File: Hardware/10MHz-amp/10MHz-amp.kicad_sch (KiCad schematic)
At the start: 122 parts, among them J1 Conn_Coaxial, J2 BANANA_JACK, J3 BANANA_JACK, J4 BANANA_JACK, J5 Conn_Coaxial, J6 Barrel_Jack_MountingPin, J7 Conn_01x07_Pin, J8 Conn_01x07_Socket, K1 TQ2-24V, K2 TQ2-24V, K3 TQ2-24V, K4 TQ2-24V, K5 TQ2-24V, K6 TQ2-5V, Q1 DMPH6250SQ-13, Q2 DMN6075SQ-7, Q4 DMPH6250SQ-13, SW1 SW_SPDT, SW2 SW_SPST, SW3 SW_SP5T_NR01105, SW5 100SP2T1B1M1QEH, U1 THS3491xDDA

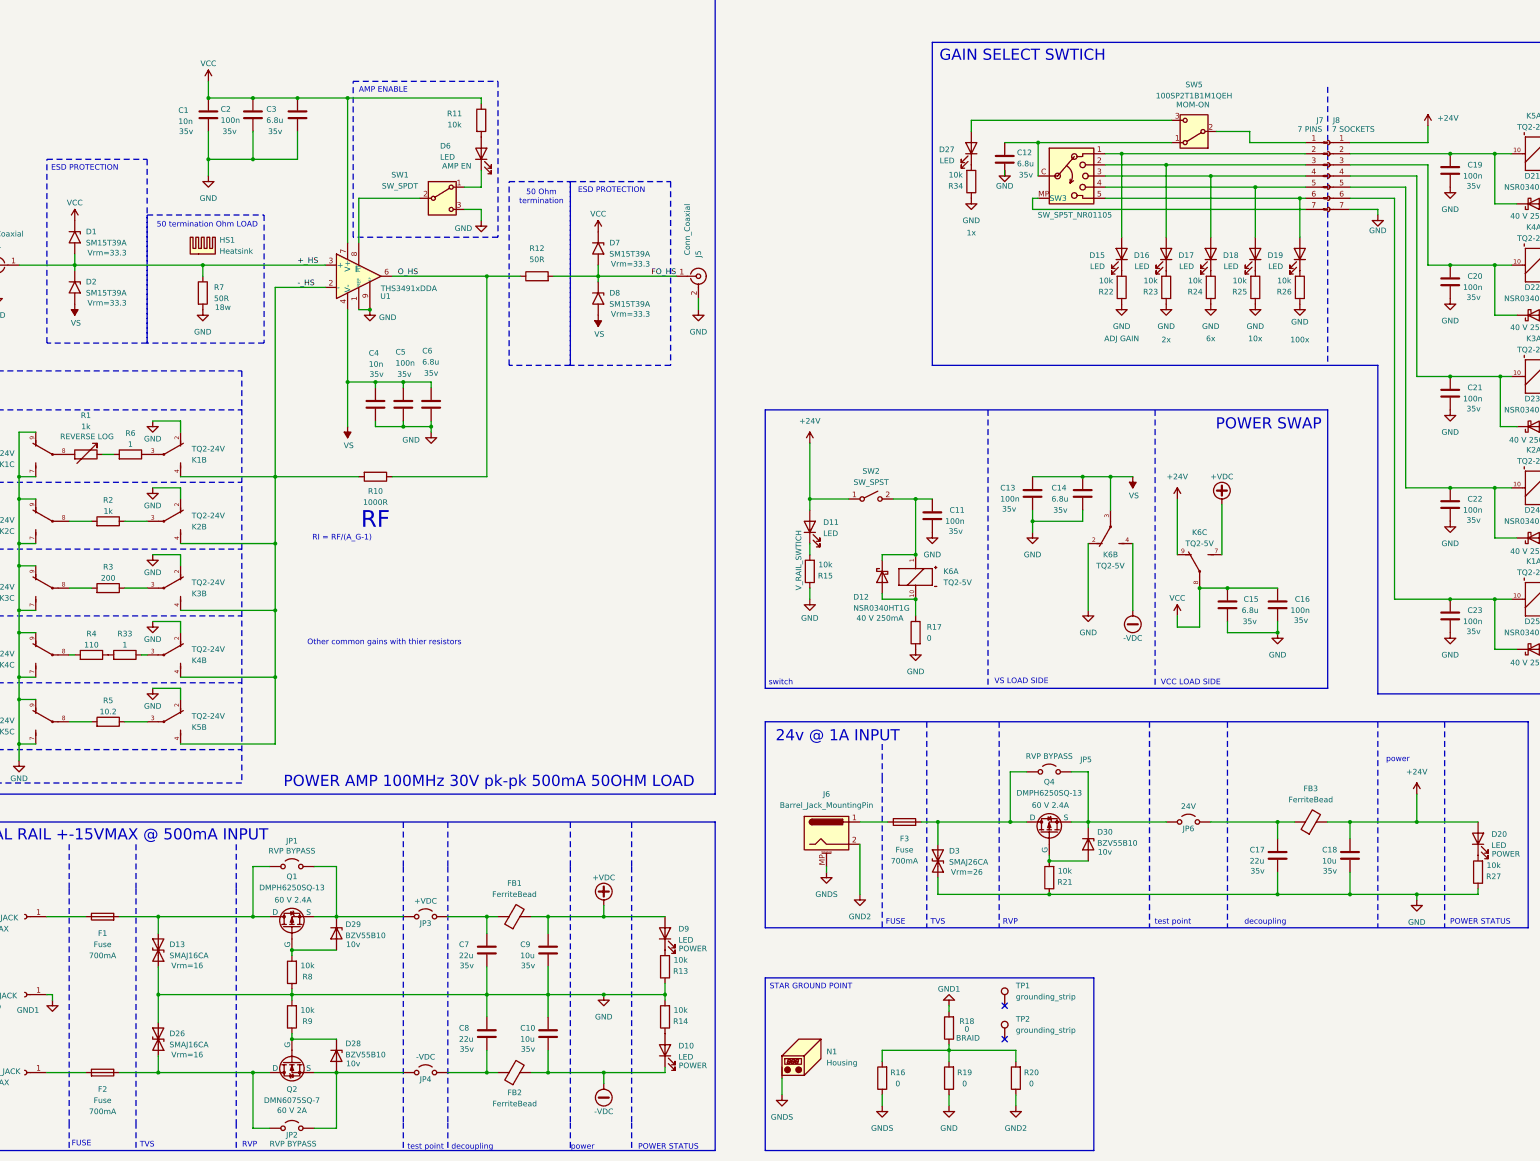
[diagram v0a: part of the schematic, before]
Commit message: changed rotary switch to a 6 pos rather then 5 and remove the switch
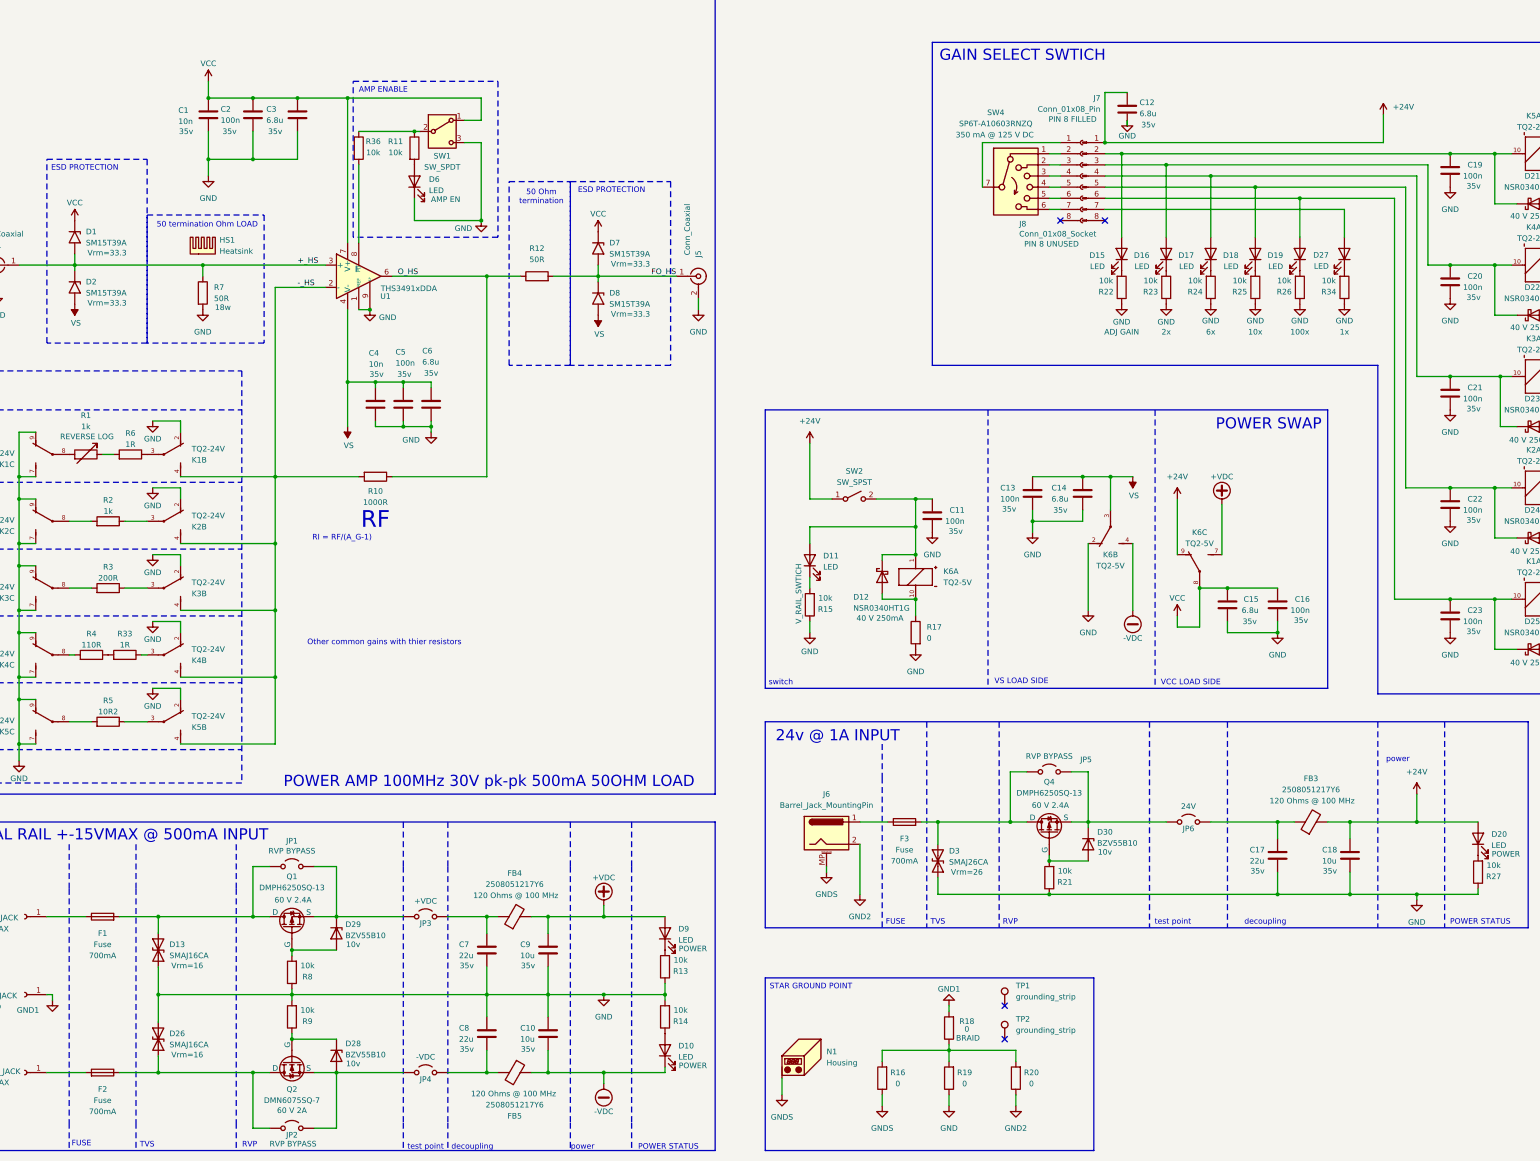
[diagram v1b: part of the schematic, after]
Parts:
- removed FB1, FB2: FerriteBead, symbol Device:FerriteBead
- removed J7: Conn_01x07_Pin, Connector_PinHeader_2.54mm:PinHeader_1x07_P2.54mm_Horizontal, symbol Connector:Conn_01x07_Pin
- removed J8: Conn_01x07_Socket, Connector_PinSocket_2.54mm:PinSocket_1x07_P2.54mm_Vertical, symbol Connector:Conn_01x07_Socket
- removed SW3: SW_SP5T_NR01105, Button_Switch_THT:SW_NKK_NR01, symbol Switch:SW_SP5T_NR01105
- removed SW5: 100SP2T1B1M1QEH, Connector_PinHeader_2.54mm:PinHeader_1x03_P2.54mm_Vertical, symbol Switch:SW_SPDT
- added FB4, FB5: 2508051217Y6, Resistor_SMD:R_0805_2012Metric, symbol Device:FerriteBead
- added J7: Conn_01x08_Pin, symbol Connector:Conn_01x08_Pin
- added J8: Conn_01x08_Socket, symbol Connector:Conn_01x08_Socket
- added R36: 10k, Capacitor_SMD:C_0603_1608Metric, symbol Device:R
- added SW4: SP6T-A10603RNZQ, Connector_PinHeader_2.54mm:PinHeader_2x04_P2.54mm_Vertical, symbol Switch:SW_Rotary_1x6_MP
- D28, D29, D30: Supplier Part Number (none) -> 1727-2646-1-ND; Supplier link (none) -> https://www.digikey.co.nz/en/products/detail/nexperia-usa-i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
- FB3: value FerriteBead -> 2508051217Y6; footprint (none) -> Resistor_SMD:R_0805_2012Metric; Manufactor Part Number (none) -> 2508051217Y6; Notes (none) -> 120 Ohms @ 100 MHz; Supplier Part Number (none) -> 1934-1472-1-ND; Supplier link (none) -> https://www.digikey.co.nz/en/products/detail/fair-rite-prod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
- Q1, Q4: Supplier Part Number (none) -> 31-DMPH6250SQ-13CT-ND
- Q2: Supplier Part Number (none) -> 31-DMN6075SQ-7CT-ND
- R3: value 200 -> 200R
- R33, R6: value 1 -> 1R
- R4: value 110 -> 110R
- R5: value 10.2 -> 10R2
- TP1, TP2: now left out of the parts list
- U1: footprint Package_SO:Texas_R-PDSO-G8_EP2.95x4.9mm_Mask2.4x3.1mm -> Package_SO:SOIC-8-1EP_3.9x4.9mm_P1.27mm_EP2.41x3.3mm; Manufactor Part Number (none) -> THS3491IDDAR; Supplier Part Number (none) -> 296-THS3491IDDARCT-ND; Supplier link (none) -> https://www.digikey.co.nz/en/products/detail/texas-instrume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
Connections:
- net +24V: now also C12.1, J7.1 (Pin_1); no longer D11.2 (A)
- net +VDC: now also FB4.2
- net -VDC: now also FB5.1
- net GND: now also D6.1 (K)
- net VCC: now also SW1.1 (A); no longer R11.1
- net at C22.1, D24.1 (K), K2.10: now also D18.2 (A), J7.5 (Pin_5)
- net at C11.1, D12.1 (K), K6.1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: now also D11.2 (A)
- net at C8.2, JP4.2 (B): now also FB5.2
- net at C19.1, D21.1 (K), K5.10: now also D15.2 (A), J7.2 (Pin_2)
- net at SW1.2 (B): now also R11.1, R36.1; no longer U1.8 (~{PD})
- net at D16.2 (A): now also C20.1, D22.1 (K), K4.10, J7.3 (Pin_3)
- net at D17.2 (A): now also C21.1, D23.1 (K), K3.10, J7.4 (Pin_4)
- net at D19.2 (A): now also C23.1, D25.1 (K), K1.10, J7.6 (Pin_6)
- net at C7.1, JP3.2 (B): now also FB4.1
- net at D27.2 (A): now also J7.7 (Pin_7)
- new net: R36.2, U1.8 (~{PD})
- new net: J8.1 (Pin_1), SW4.7
- new net: J8.2 (Pin_2), SW4.1
- new net: J8.3 (Pin_3), SW4.2
- new net: J8.4 (Pin_4), SW4.3
- new net: J8.5 (Pin_5), SW4.4
- new net: J8.6 (Pin_6), SW4.5
- new net: J8.7 (Pin_7), SW4.6
- no-connect marks 2 -> 4
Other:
- moved on the sheet: C12, D11, D27, D6, R11, R15, R34, SW1, SW2

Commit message: made all switches pannel mount and add pcb connectors for them
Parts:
- removed SW2: SW_SPST, symbol Switch:SW_SPST
- added J10, J12, J13: Conn_01x03_Socket, symbol Connector:Conn_01x03_Socket
- added J11, J14, J9: Conn_01x03_Pin, symbol Connector:Conn_01x03_Pin
- added SW2, SW3: SW_SPDT, symbol Switch:SW_SPDT
- J8: footprint (none) -> Connector_PinHeader_2.54mm:PinHeader_2x04_P2.54mm_Vertical; Manufactor Part Number (none) -> PPTC042LFBN-RC; Supplier Part Number (none) -> S7072-ND; Supplier link (none) -> https://www.digikey.co.nz/en/products/detail/sullins-connec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
- K6: value TQ2-5V -> TQ2-24V; Manufactor Part Number (none) -> TQ2-24V; Notes (none) -> 12.5 mA; Supplier Part Number (none) -> TQ2-24V; Supplier link (none) -> https://www.digikey.ca/en/products/detail/panasonic-electri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
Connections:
- net +24V: now also J12.1 (Pin_1)
- net GND: now also J10.3 (Pin_3), J12.3 (Pin_3), J13.1 (Pin_1); no longer SW1.3 (C)
- net VCC: now also J10.1 (Pin_1); no longer SW1.1 (A)
- net at C11.1, D11.2 (A), D12.1 (K)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: now also J12.2 (Pin_2)
- net at F3.1: now also J13.2 (Pin_2); no longer J6.1
- net at R11.1, R36.1: now also J10.2 (Pin_2); no longer SW1.2 (B)
- new net: J9.1 (Pin_1), SW1.1 (A)
- new net: J9.2 (Pin_2), SW1.2 (B)
- new net: J9.3 (Pin_3), SW1.3 (C)
- new net: J13.3 (Pin_3), J6.1
- new net: J14.1 (Pin_1), SW3.1 (A)
- new net: J14.2 (Pin_2), SW3.2 (B)
- new net: J14.3 (Pin_3), SW3.3 (C)
- new net: J11.1 (Pin_1), SW2.1 (A)
- new net: J11.2 (Pin_2), SW2.2 (B)
- new net: J11.3 (Pin_3), SW2.3 (C)
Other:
- moved on the sheet: C1, C10, C11, C12, C13, C14, C15, C16, C17, C18, C19, C2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

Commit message: added footprints to everything but the resistors
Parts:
- removed J11: Conn_01x03_Pin, symbol Connector:Conn_01x03_Pin
- removed J12: Conn_01x03_Socket, symbol Connector:Conn_01x03_Socket
- added J5: 1x03_Socket, Connector_Molex:Molex_KK-396_5273-03A_1x03_P3.96mm_Vertical, symbol Connector:Conn_01x03_Socket
- added J6: Conn_01x03_Pin, symbol Connector:Conn_01x03_Pin
- added TP10, TP11, TP3, TP4, TP5, TP6, TP7, TP8, TP9: crimp, symbol Connector:TestPoint
- C1, C4: Manufactor Part Number (none) -> C0603C103K5RACTU; Notes 35v -> 50v; Supplier Part Number (none) -> 399-C0603C103K5RACTUCT-ND; Supplier link (none) -> https://www.digikey.co.nz/en/products/detail/kemet/C0603C10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
- C10, C18, C9: Manufactor Part Number (none) -> HHXC630ARA100MF61G; Notes 35v -> 63V; Supplier Part Number (none) -> 565-4787-1-ND; Supplier link (none) -> https://www.digikey.co.nz/en/products/detail/chemi-con/HHXC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
- C11, C16, C19, C2, C20, C21, C22, C23, C5: footprint Capacitor_SMD:C_0603_1608Metric -> Capacitor_SMD:C_0805_2012Metric; Manufactor Part Number (none) -> C0805C104K5RACTU; Notes 35v -> 50v; Supplier Part Number (none) -> 399-C0805C104K5RACTUCT-ND; Supplier link (none) -> https://www.digikey.co.nz/en/products/detail/kemet/C0805C10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
- C12: renamed from C13; footprint Capacitor_SMD:C_0603_1608Metric -> Capacitor_SMD:C_0805_2012Metric; Manufactor Part Number (none) -> C0805C104K5RACTU; Notes 35v -> 50v; Supplier Part Number (none) -> 399-C0805C104K5RACTUCT-ND; Supplier link (none) -> https://www.digikey.co.nz/en/products/detail/kemet/C0805C10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
- C13: renamed from C14; footprint Capacitor_SMD:C_0603_1608Metric -> Capacitor_SMD:C_1812_4532Metric; Manufactor Part Number (none) -> C4532X7R1H685K250KB; Notes 35v -> 50v; Supplier Part Number (none) -> 445-3919-1-ND; Supplier link (none) -> https://www.digikey.co.nz/en/products/detail/tdk-corporatio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
- C14: renamed from C12; footprint Capacitor_SMD:C_0603_1608Metric -> Capacitor_SMD:C_1812_4532Metric; Manufactor Part Number (none) -> C4532X7R1H685K250KB; Notes 35v -> 50v; Supplier Part Number (none) -> 445-3919-1-ND; Supplier link (none) -> https://www.digikey.co.nz/en/products/detail/tdk-corporatio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
- C15, C3, C6: footprint Capacitor_SMD:C_0603_1608Metric -> Capacitor_SMD:C_1812_4532Metric; Manufactor Part Number (none) -> C4532X7R1H685K250KB; Notes 35v -> 50v; Supplier Part Number (none) -> 445-3919-1-ND; Supplier link (none) -> https://www.digikey.co.nz/en/products/detail/tdk-corporatio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
- C17, C7, C8: footprint Capacitor_SMD:C_0603_1608Metric -> Capacitor_SMD:CP_Elec_6.3x7.7; Manufactor Part Number (none) -> A768EB226M1HLAE048; Notes 35v -> 50v; Supplier Part Number (none) -> 399-A768EB226M1HLAE048CT-ND; Supplier link (none) -> https://www.digikey.co.nz/en/products/detail/kemet/A768EB22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
- D10: renamed from D9; footprint Diode_SMD:D_0603_1608Metric -> LED_THT:LED_D5.0mm_Horizontal_O6.35mm_Z3.0mm; Manufactor Part Number (none) -> WP7113ID; Supplier Part Number (none) -> 754-1264-ND; Supplier link (none) -> https://www.digikey.co.nz/en/products/detail/kingbright/WP7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
- D11: renamed from D10; footprint Diode_SMD:D_0603_1608Metric -> LED_THT:LED_D5.0mm_Horizontal_O6.35mm_Z3.0mm; Manufactor Part Number (none) -> WP7113ID; Supplier Part Number (none) -> 754-1264-ND; Supplier link (none) -> https://www.digikey.co.nz/en/products/detail/kingbright/WP7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
- D12: renamed from D11; footprint Diode_SMD:D_0603_1608Metric -> LED_THT:LED_D5.0mm_Horizontal_O6.35mm_Z3.0mm; Manufactor Part Number (none) -> WP7113ID; Supplier Part Number (none) -> 754-1264-ND; Supplier link (none) -> https://www.digikey.co.nz/en/products/detail/kingbright/WP7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
- D14: renamed from D3; Manufactor Part Number (none) -> SMAJ26CA; Supplier Part Number (none) -> 18-SMAJ26CACT-ND; Supplier link (none) -> https://www.digikey.co.nz/en/products/detail/littelfuse-inc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
- D15: footprint Diode_SMD:D_0603_1608Metric -> LED_THT:LED_D5.0mm_Horizontal_O6.35mm_Z3.0mm; Manufactor Part Number (none) -> WP7113ID; Supplier Part Number (none) -> 754-1264-ND; Supplier link (none) -> https://www.digikey.co.nz/en/products/detail/kingbright/WP7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
- D17: renamed from D16; footprint Diode_SMD:D_0603_1608Metric -> LED_THT:LED_D5.0mm_Horizontal_O6.35mm_Z3.0mm; Manufactor Part Number (none) -> WP7113ID; Supplier Part Number (none) -> 754-1264-ND; Supplier link (none) -> https://www.digikey.co.nz/en/products/detail/kingbright/WP7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
- D18: renamed from D17; footprint Diode_SMD:D_0603_1608Metric -> LED_THT:LED_D5.0mm_Horizontal_O6.35mm_Z3.0mm; Manufactor Part Number (none) -> WP7113ID; Supplier Part Number (none) -> 754-1264-ND; Supplier link (none) -> https://www.digikey.co.nz/en/products/detail/kingbright/WP7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
- D19: renamed from D18; footprint Diode_SMD:D_0603_1608Metric -> LED_THT:LED_D5.0mm_Horizontal_O6.35mm_Z3.0mm; Manufactor Part Number (none) -> WP7113ID; Supplier Part Number (none) -> 754-1264-ND; Supplier link (none) -> https://www.digikey.co.nz/en/products/detail/kingbright/WP7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
- D20: renamed from D19; footprint Diode_SMD:D_0603_1608Metric -> LED_THT:LED_D5.0mm_Horizontal_O6.35mm_Z3.0mm; Manufactor Part Number (none) -> WP7113ID; Supplier Part Number (none) -> 754-1264-ND; Supplier link (none) -> https://www.digikey.co.nz/en/products/detail/kingbright/WP7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
- D21: renamed from D27; footprint Diode_SMD:D_0603_1608Metric -> LED_THT:LED_D5.0mm_Horizontal_O6.35mm_Z3.0mm; Manufactor Part Number (none) -> WP7113ID; Supplier Part Number (none) -> 754-1264-ND; Supplier link (none) -> https://www.digikey.co.nz/en/products/detail/kingbright/WP7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
- D27: renamed from D20; footprint Diode_SMD:D_0603_1608Metric -> LED_THT:LED_D5.0mm_Horizontal_O6.35mm_Z3.0mm; Manufactor Part Number (none) -> WP7113ID; Supplier Part Number (none) -> 754-1264-ND; Supplier link (none) -> https://www.digikey.co.nz/en/products/detail/kingbright/WP7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
- D3: renamed from D13; Manufactor Part Number (none) -> SMAJ16CA; Supplier Part Number (none) -> SMAJ16CABCT-ND; Supplier link (none) -> https://www.digikey.co.nz/en/products/detail/bourns-inc/SMA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
- D4: renamed from D26; Manufactor Part Number (none) -> SMAJ16CA; Supplier Part Number (none) -> SMAJ16CABCT-ND; Supplier link (none) -> https://www.digikey.co.nz/en/products/detail/bourns-inc/SMA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
- D7: renamed from D6; footprint Diode_SMD:D_0603_1608Metric -> LED_THT:LED_D5.0mm_Horizontal_O6.35mm_Z3.0mm; Manufactor Part Number (none) -> WP7113ID; Supplier Part Number (none) -> 754-1264-ND; Supplier link (none) -> https://www.digikey.co.nz/en/products/detail/kingbright/WP7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
- F1, F2: footprint (none) -> MountingHole:MountingHole_3mm_Pad_Via; Manufactor Part Number (none) -> BK/HTB-46I-R; Supplier Part Number (none) -> 283-BK/HTB-46I-R-ND; Supplier link (none) -> https://www.digikey.co.nz/en/products/detail/eaton-electron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
- F3: Manufactor Part Number (none) -> BK/HTB-46I-R; Supplier Part Number (none) -> 283-BK/HTB-46I-R-ND; Supplier link (none) -> https://www.digikey.co.nz/en/products/detail/eaton-electron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
- J1: footprint (none) -> Connector_Coaxial:BNC_TEConnectivity_1478035_Horizontal; Manufactor Part Number (none) -> 112659; Notes (none) -> BNC; Supplier Part Number (none) -> 115-112659-ND; Supplier link (none) -> https://www.digikey.co.nz/en/products/detail/amphenol-rf/11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
- J10: value Conn_01x03_Socket -> 1x03_Socket; footprint (none) -> Connector_Molex:Molex_KK-396_5273-03A_1x03_P3.96mm_Vertical; Manufactor Part Number (none) -> 0026604030; Notes (none) -> KK-396; Supplier Part Number (none) -> WM4621-ND; Supplier link (none) -> https://www.digikey.co.nz/en/products/detail/molex/00266040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
- J11: renamed from J13; value Conn_01x03_Socket -> 1x03_Socket; footprint (none) -> Connector_Molex:Molex_KK-396_5273-03A_1x03_P3.96mm_Vertical; Manufactor Part Number (none) -> 0026604030; Notes (none) -> KK-396; Supplier Part Number (none) -> WM4621-ND; Supplier link (none) -> https://www.digikey.co.nz/en/products/detail/molex/00266040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
- J12: renamed from J14; value Conn_01x03_Pin -> 01x03_Pin; Manufactor Part Number (none) -> 0009503031; Notes (none) -> kk-396; Supplier Part Number (none) -> WM2101-ND; Supplier link (none) -> https://www.digikey.co.nz/en/products/detail/molex/00095030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
- J13: renamed from J8; footprint Connector_PinHeader_2.54mm:PinHeader_2x04_P2.54mm_Vertical -> (none)
- J14: renamed from J7; footprint (none) -> Connector_PinHeader_2.54mm:PinHeader_2x04_P2.54mm_Vertical; Manufactor Part Number (none) -> TSW-104-07-F-D; Supplier Part Number (none) -> SAM8996-ND; Supplier link (none) -> https://www.digikey.ca/en/products/detail/samtec-inc/TSW-10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
- J2: Manufactor Part Number (none) -> 5931-2; Notes +15V MAX -> +15V MAX, RED; Supplier Part Number (none) -> 501-1879-ND; Supplier link (none) -> https://www.digikey.co.nz/en/products/detail/pomona-electro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
- J3: Manufactor Part Number (none) -> 5931-0; Notes GND -> GND, BLACK; Supplier Part Number (none) -> 501-1805-ND; Supplier link (none) -> https://www.digikey.co.nz/en/products/detail/pomona-electro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
- J4: Manufactor Part Number (none) -> 5931-6; Notes -15V MAX -> -15V MAX, BLUE; Supplier Part Number (none) -> 501-1925-ND; Supplier link (none) -> https://www.digikey.co.nz/en/products/detail/pomona-electro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
- J7: renamed from J5; footprint (none) -> Connector_Coaxial:BNC_TEConnectivity_1478035_Horizontal; Manufactor Part Number (none) -> 112659; Notes (none) -> BNC; Supplier Part Number (none) -> 115-112659-ND; Supplier link (none) -> https://www.digikey.co.nz/en/products/detail/amphenol-rf/11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
- J8: renamed from J6; value Barrel_Jack_MountingPin -> PJ-063AH; footprint (none) -> Connector_BarrelJack:BarrelJack_CUI_PJ-063AH_Horizontal; Manufactor Part Number (none) -> PJ-063AH; Notes (none) -> 24v @ 1A, 5.5mm; Supplier Part Number (none) -> CP-063AH-ND; Supplier link (none) -> https://www.digikey.ca/en/products/detail/same-sky-formerly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
- J9: Manufactor Part Number (none) -> 0009503031; Notes (none) -> kk-396; Supplier Part Number (none) -> WM2101-ND; Supplier link (none) -> https://www.digikey.co.nz/en/products/detail/molex/00095030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
- JP1, JP2, JP4, JP5, JP6: footprint (none) -> Jumper:SolderJumper-2_P1.3mm_Open_TrianglePad1.0x1.5mm
- JP3: footprint (none) -> Jumper:SolderJumper-2_P1.3mm_Open_TrianglePad1.0x1.5mm; now in the parts list
- N1: Manufactor Part Number (none) -> EXN-23357-BL; Notes (none) -> BLUE; Supplier Part Number (none) -> 377-2523-ND; Supplier link (none) -> https://www.digikey.co.nz/en/products/detail/bud-industries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
- R10: renamed from R9; footprint Capacitor_SMD:C_0603_1608Metric -> Resistor_SMD:R_0603_1608Metric
- R11: renamed from R36; footprint Capacitor_SMD:C_0603_1608Metric -> Resistor_SMD:R_0603_1608Metric
- R12: renamed from R10; footprint Capacitor_SMD:C_0603_1608Metric -> Resistor_SMD:R_0603_1608Metric
- R13: renamed from R11; footprint Capacitor_SMD:C_0603_1608Metric -> Resistor_SMD:R_0603_1608Metric
- R14: renamed from R12; footprint Capacitor_SMD:C_0603_1608Metric -> Resistor_SMD:R_0603_1608Metric
- R15: renamed from R13; footprint Capacitor_SMD:C_0603_1608Metric -> Resistor_SMD:R_0603_1608Metric
- R16: renamed from R14; footprint Capacitor_SMD:C_0603_1608Metric -> Resistor_SMD:R_0603_1608Metric
- R17: renamed from R15; footprint Capacitor_SMD:C_0603_1608Metric -> Resistor_SMD:R_0603_1608Metric
- R18: renamed from R16; footprint (none) -> Resistor_SMD:R_0603_1608Metric
- R19: renamed from R17; footprint Capacitor_SMD:C_0603_1608Metric -> Resistor_SMD:R_0603_1608Metric
- R2: renamed from R4; footprint Capacitor_SMD:C_0603_1608Metric -> Resistor_SMD:R_0603_1608Metric
- R20: renamed from R18; footprint (none) -> Resistor_SMD:R_0603_1608Metric
- R21: renamed from R19; footprint (none) -> Resistor_SMD:R_0603_1608Metric
- R22: renamed from R20; footprint (none) -> Resistor_SMD:R_0603_1608Metric
- R23: renamed from R22; footprint Capacitor_SMD:C_0603_1608Metric -> Resistor_SMD:R_0603_1608Metric
- R24: renamed from R21; footprint Capacitor_SMD:C_0603_1608Metric -> Resistor_SMD:R_0603_1608Metric
- R25: renamed from R23; footprint Capacitor_SMD:C_0603_1608Metric -> Resistor_SMD:R_0603_1608Metric
- R26: renamed from R24; footprint Capacitor_SMD:C_0603_1608Metric -> Resistor_SMD:R_0603_1608Metric
- R27: renamed from R25; footprint Capacitor_SMD:C_0603_1608Metric -> Resistor_SMD:R_0603_1608Metric
- R28: renamed from R26; footprint Capacitor_SMD:C_0603_1608Metric -> Resistor_SMD:R_0603_1608Metric
- R29: renamed from R34; footprint Capacitor_SMD:C_0603_1608Metric -> Resistor_SMD:R_0603_1608Metric
- R3: renamed from R2; footprint Capacitor_SMD:C_0603_1608Metric -> Resistor_SMD:R_0603_1608Metric
- R30: renamed from R27; footprint Capacitor_SMD:C_0603_1608Metric -> Resistor_SMD:R_0603_1608Metric
- R31: renamed from R28; footprint Capacitor_SMD:C_0603_1608Metric -> Resistor_SMD:R_0603_1608Metric
- R32: renamed from R29; footprint Capacitor_SMD:C_0603_1608Metric -> Resistor_SMD:R_0603_1608Metric
- R33: renamed from R30; footprint Capacitor_SMD:C_0603_1608Metric -> Resistor_SMD:R_0603_1608Metric
- R34: renamed from R31; footprint Capacitor_SMD:C_0603_1608Metric -> Resistor_SMD:R_0603_1608Metric
- R35: renamed from R32; footprint Capacitor_SMD:C_0603_1608Metric -> Resistor_SMD:R_0603_1608Metric
- R4: renamed from R3; footprint Capacitor_SMD:C_0603_1608Metric -> Resistor_SMD:R_0603_1608Metric
- R5: footprint Capacitor_SMD:C_0603_1608Metric -> Resistor_SMD:R_0603_1608Metric
- R6: renamed from R33; footprint Capacitor_SMD:C_0603_1608Metric -> Resistor_SMD:R_0603_1608Metric
- R7: renamed from R6; footprint Capacitor_SMD:C_0603_1608Metric -> Resistor_SMD:R_0603_1608Metric
- R8: renamed from R7; footprint Capacitor_SMD:C_0603_1608Metric -> Resistor_SMD:R_0603_1608Metric
- R9: renamed from R8; footprint Capacitor_SMD:C_0603_1608Metric -> Resistor_SMD:R_0603_1608Metric
- SW1: Manufactor Part Number (none) -> ANT11SECQE; Notes (none) -> AMP EN; Supplier Part Number (none) -> 2449-ANT11SECQE-ND; Supplier link (none) -> https://www.digikey.co.nz/en/products/detail/cit-relay-and-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
- SW2: Manufactor Part Number (none) -> ANT11SECQE; Notes (none) -> PWR; Supplier Part Number (none) -> 2449-ANT11SECQE-ND; Supplier link (none) -> https://www.digikey.co.nz/en/products/detail/cit-relay-and-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
- SW3: Manufactor Part Number (none) -> ANT11SECQE; Supplier Part Number (none) -> 2449-ANT11SECQE-ND; Supplier link (none) -> https://www.digikey.co.nz/en/products/detail/cit-relay-and-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
- renumbered D12 to D13, D30 to D16, D21 to D22, D22 to D23, D23 to D24, D24 to D25, D25 to D26, D29 to D5, D28 to D6, D7 to D8, D8 to D9, FB4 to FB1, FB5 to FB2, Q4 to Q3
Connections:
- net +24V: now also J10.3 (Pin_3)
- net GND: now also J10.1 (Pin_1), J5.1 (Pin_1); no longer J10.3 (Pin_3)
- net VCC: now also J5.3 (Pin_3); no longer J10.1 (Pin_1)
- net at C11.1, D12.2 (A), D13.1 (K)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: now also J10.2 (Pin_2)
- net at SW1.1 (A): now also J6.3 (Pin_3); no longer J9.1 (Pin_1)
- net at SW1.2 (B): now also J6.2 (Pin_2); no longer J9.2 (Pin_2)
- net at SW1.3 (C): now also J6.1 (Pin_1); no longer J9.3 (Pin_3)
- net at F3.1: now also J11.3 (Pin_3); no longer J11.2 (Pin_2)
- net at D14.2 (A2), JP5.1 (A), Q3.1 (D): now also J11.2 (Pin_2); no longer F3.2
- net at J8.1: now also F3.2; no longer J11.3 (Pin_3)
- net at R11.1, R13.1: now also J5.2 (Pin_2); no longer J10.2 (Pin_2)
- net at SW2.1 (A): now also J9.3 (Pin_3)
- net at SW2.2 (B): now also J9.2 (Pin_2)
- net at SW2.3 (C): now also J9.1 (Pin_1)
- no-connect marks 4 -> 13
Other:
- note added: "DECOUPLING"
- note added: "NOTES:"
- note added: "ONLY ONE POWER SWITCH IS NEEDED AS WHEN THE 24V IS DISCONNECTED THE RELAYS IN THE "POWER SWAP" CIRCUIT WILL SWAP BACK TO THE NC STATE WHICH IS CONNECTED TO 24V AND GND"
- note added: "POWER"
- note added: "SWITCH"
- note added: "TEST POINT"
- note added: "THE BANANA JACK AND FUSES ARE ALL PANEL MOUNTED, AND THERE FOR THE FUSE SYMBOL IS USED TO STORE THE FOOT PRINT FOR THE ON BOARD CONNECTION"
- note added: "WHERE YOU SEE PINS AND SOCKETS NEXT TO EACH OTHER ELUDES TO THE FACT THE COMPONENT ON THE OTHER SIDE WILL BE PANEL MOUNT"
- note added: "crimps for the modelx connectors"
- moved on the sheet: C10, C11, C12, C13, C15, C16, C17, C18, C7, C8, C9, D10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

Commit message: added more datasheets
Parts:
- renumbered R3 to R2, R4 to R3, R2 to R4
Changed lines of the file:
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@@
 	(wire
 		(pts
-			(xy 50.8 130.81) (xy 45.72 130.81)
-		)
-		(stroke
-			(width 0)
-			(type default)
-		)
-	)
-	(wire
-		(pts
 			(xy 151.13 222.25) (xy 154.94 222.25)
 		)
@@
 	(wire
 		(pts
+			(xy 50.8 130.81) (xy 45.72 130.81)
+		)
+		(stroke
+			(width 0)
+			(type default)
+		)
+	)
+	(wire
+		(pts
 			(xy 34.29 135.89) (xy 34.29 125.73)
 		)
@@
 	(wire
 		(pts
+			(xy 50.8 146.05) (xy 45.72 146.05)
+		)
+		(stroke
+			(width 0)
+			(type default)
+		)
+	)
+	(wire
+		(pts
 			(xy 167.64 219.71) (xy 167.64 222.25)
 		)
@@
 	(wire
 		(pts
-			(xy 50.8 146.05) (xy 45.72 146.05)
-		)
-		(stroke
-			(width 0)
-			(type default)
-		)
-	)
-	(wire
-		(pts
 			(xy 119.38 74.93) (xy 140.97 74.93)
 		)
@@
 		(on_board yes)
 		(dnp no)
-		(property "Reference" "R2"
+		(property "Reference" "R4"
 			(at 50.8 156.464 90)
 			(effects
@@
 			(project "10MHz-amp"
 				(path "/4f1bcd0b-e27d-4d3c-bb56-f1e153ba9c72"
-					(reference "R2")
+					(reference "R4")
 					(unit 1)
 				)
@@
 		(on_board yes)
 		(dnp no)
-		(property "Reference" "R3"
+		(property "Reference" "R2"
 			(at 54.61 125.984 90)
 			(effects
@@
 			(project "10MHz-amp"
 				(path "/4f1bcd0b-e27d-4d3c-bb56-f1e153ba9c72"
-					(reference "R3")
+					(reference "R2")
 					(unit 1)
 				)
@@
 		(on_board yes)
 		(dnp no)
-		(property "Reference" "R4"
+		(property "Reference" "R3"
 			(at 54.61 141.224 90)
 			(effects
@@
 			(project "10MHz-amp"
 				(path "/4f1bcd0b-e27d-4d3c-bb56-f1e153ba9c72"
-					(reference "R4")
+					(reference "R3")
 					(unit 1)
 				)
